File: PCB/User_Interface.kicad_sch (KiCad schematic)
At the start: 21 parts, among them J5 Test Point, SW1 SW_Push, SW2 SW_Push, SW3 SW_Push, SW4 SW_Push, U5 NHD-C0220BIZ

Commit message: Added datasheets and PCB files
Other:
- company: (none) -> Team 18
- title: (none) -> User Interface

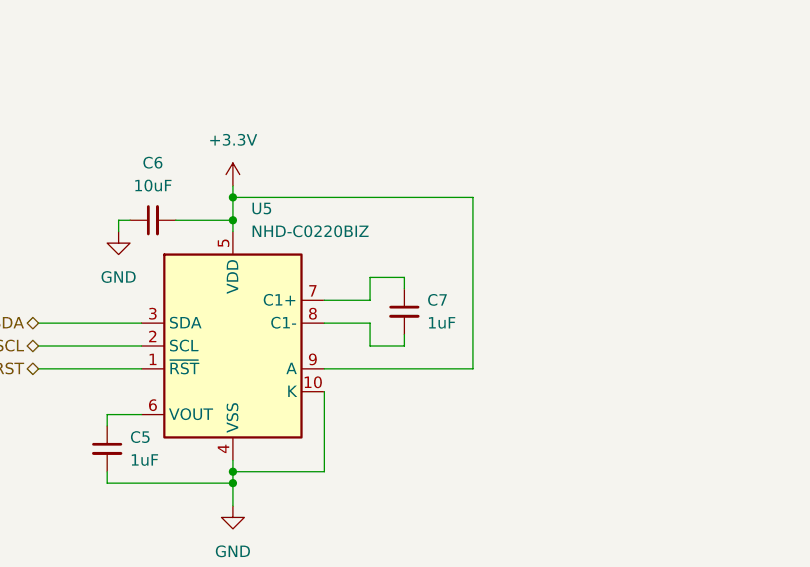
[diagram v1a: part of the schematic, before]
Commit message: Changed microcontroller from ESP32-S3 to ESP32 and added UART bridge
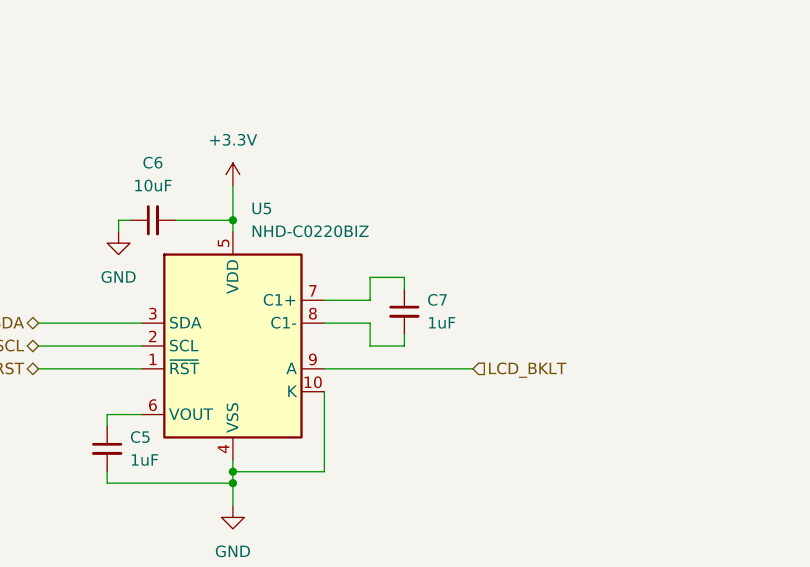
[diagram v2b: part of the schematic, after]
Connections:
- net +3.3V: no longer U5.9 (A)
- new net LCD_BKLT: U5.9 (A)
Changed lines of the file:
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@@
   (junction (at 237.49 78.74) (diameter 0) (color 0 0 0 0)
   )
-  (junction (at 81.28 46.99) (diameter 0) (color 0 0 0 0)
-  )
   (junction (at 175.26 86.36) (diameter 0) (color 0 0 0 0)
   )
@@
     (stroke (width 0) (type default))
   )
-  (wire (pts (xy 107.95 46.99) (xy 81.28 46.99))
-    (stroke (width 0) (type default))
-  )
   (wire (pts (xy 73.66 151.13) (xy 80.01 151.13))
     (stroke (width 0) (type default))
@@
     (stroke (width 0) (type default))
   )
-  (wire (pts (xy 81.28 46.99) (xy 81.28 49.53))
+  (wire (pts (xy 81.28 45.72) (xy 81.28 49.53))
     (stroke (width 0) (type default))
   )
@@
     (stroke (width 0) (type default))
   )
-  (wire (pts (xy 81.28 45.72) (xy 81.28 46.99))
-    (stroke (width 0) (type default))
-  )
   (wire (pts (xy 67.31 71.12) (xy 67.31 72.39))
     (stroke (width 0) (type default))
@@
   )
   (wire (pts (xy 200.66 55.88) (xy 201.93 55.88))
-    (stroke (width 0) (type default))
-  )
-  (wire (pts (xy 107.95 66.04) (xy 107.95 46.99))
     (stroke (width 0) (type default))
   )
@@
     (effects (font (size 1.27 1.27)) (justify right))
   )
+  (hierarchical_label "LCD_BKLT" (shape input) (at 107.95 66.04 0) (fields_autoplaced)
+    (effects (font (size 1.27 1.27)) (justify left))
+  )
   (hierarchical_label "DISP_RST" (shape bidirectional) (at 59.69 66.04 180) (fields_autoplaced)

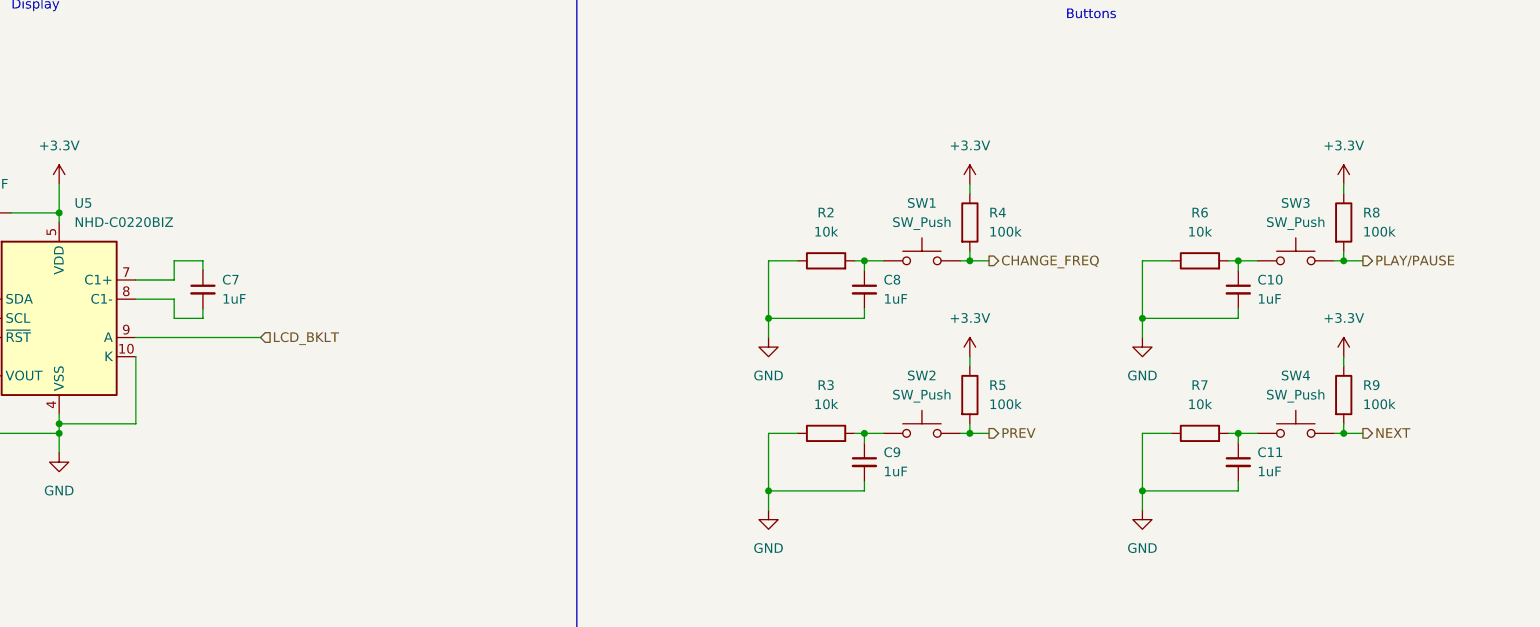
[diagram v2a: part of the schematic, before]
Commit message: Completed PCB Rev 2. Changed microcontroller to ESP32-WROOM-32, added UART bridge, removed button pull-up resistors, added I2S test point, added option to control backlight, and better organized all traces
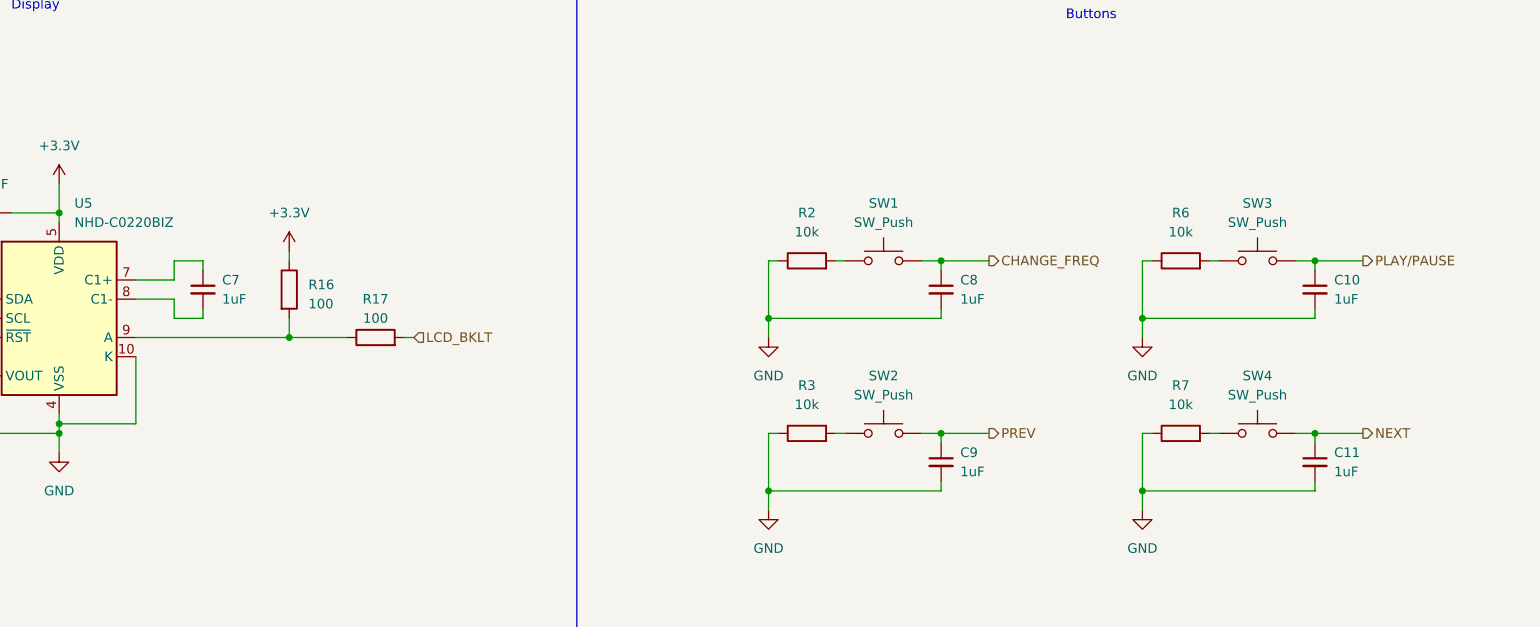
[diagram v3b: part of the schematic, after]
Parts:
- removed R4, R5, R8, R9: 100k, Resistor_SMD:R_0805_2012Metric_Pad1.20x1.40mm_HandSolder, symbol Device:R
- added R16, R17: 100, Resistor_SMD:R_0805_2012Metric_Pad1.20x1.40mm_HandSolder, symbol Device:R
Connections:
- net +3.3V: now also R16.1
- net CHANGE_FREQ: now also C8.1
- net LCD_BKLT: now also R17.2; no longer U5.9 (A)
- net NEXT: now also C11.1
- net PLAY/PAUSE: now also C10.1
- net PREV: now also C9.1
- net at R3.2, SW2.1: no longer C9.1
- net at R6.2, SW3.1: no longer C10.1
- net at R2.2, SW1.1: no longer C8.1
- net at R7.2, SW4.1: no longer C11.1
- new net: R16.2, R17.1, U5.9 (A)
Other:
- moved on the sheet: C10, C11, C8, C9, R2, R3, R6, R7, SW1, SW2, SW3, SW4

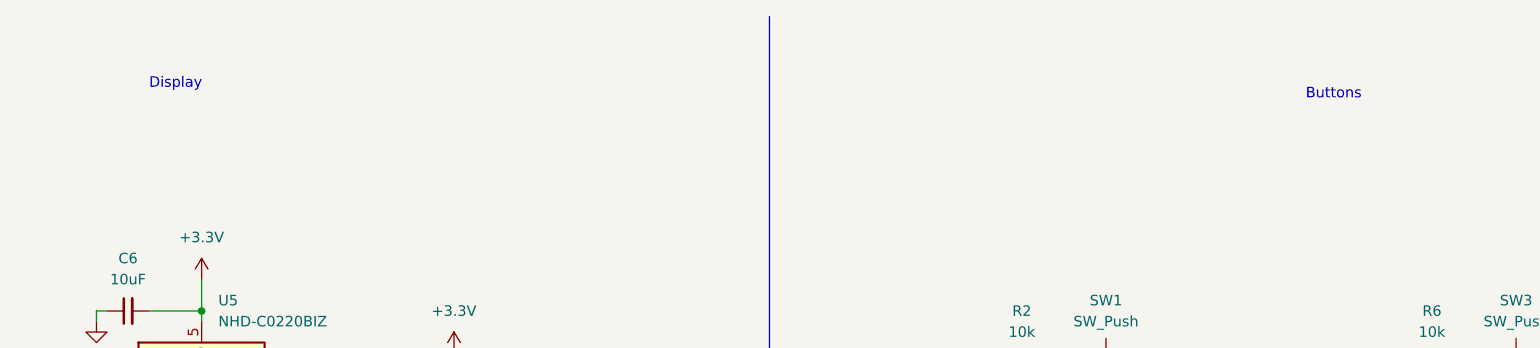
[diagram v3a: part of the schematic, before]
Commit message: Changed schematic to reflect final design
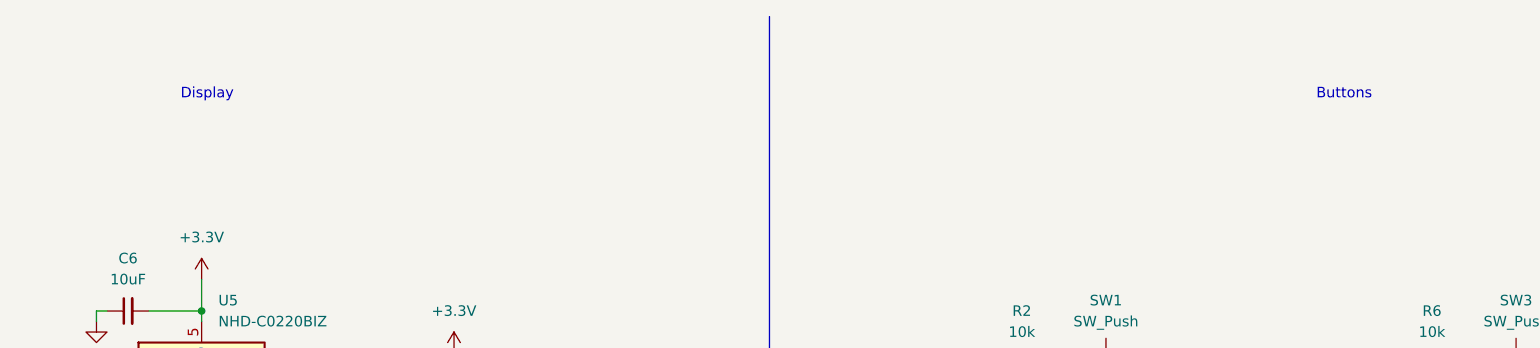
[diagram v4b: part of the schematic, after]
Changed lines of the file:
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@@
   (title_block
     (title "User Interface")
-    (date "2023-03-04")
-    (rev "2")
+    (date "2023-04-29")
+    (rev "2.2")
     (company "Team 18")
   )
@@
     (stroke (width 0) (type default))
   )
-  (text "Display" (at 74.93 22.86 0)
+  (text "Display" (at 78.74 24.13 0)
     (effects (font (size 1.27 1.27)) (justify left bottom))
   )
@@
     (effects (font (size 1.27 1.27)) (justify left bottom))
   )
-  (text "Buttons" (at 214.63 24.13 0)
+  (text "Buttons" (at 215.9 24.13 0)
     (effects (font (size 1.27 1.27)) (justify left bottom))
   )
